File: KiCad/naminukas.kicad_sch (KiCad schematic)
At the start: 13 parts

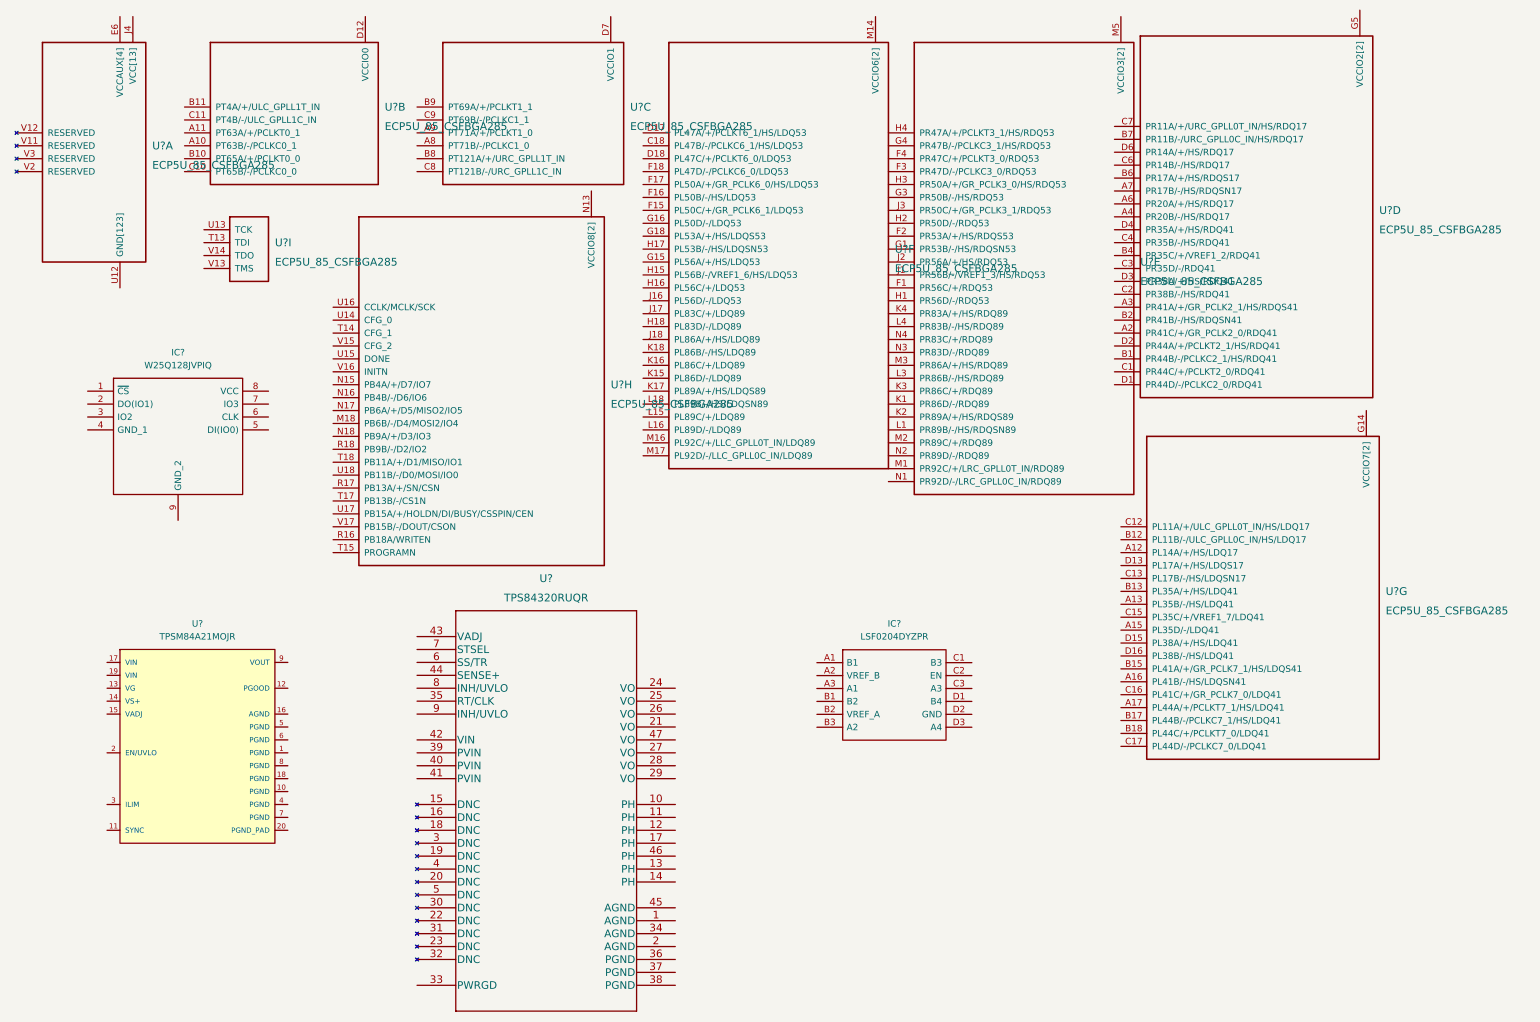
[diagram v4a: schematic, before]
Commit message: Split schematic as both FPGA and power module symbols are huge
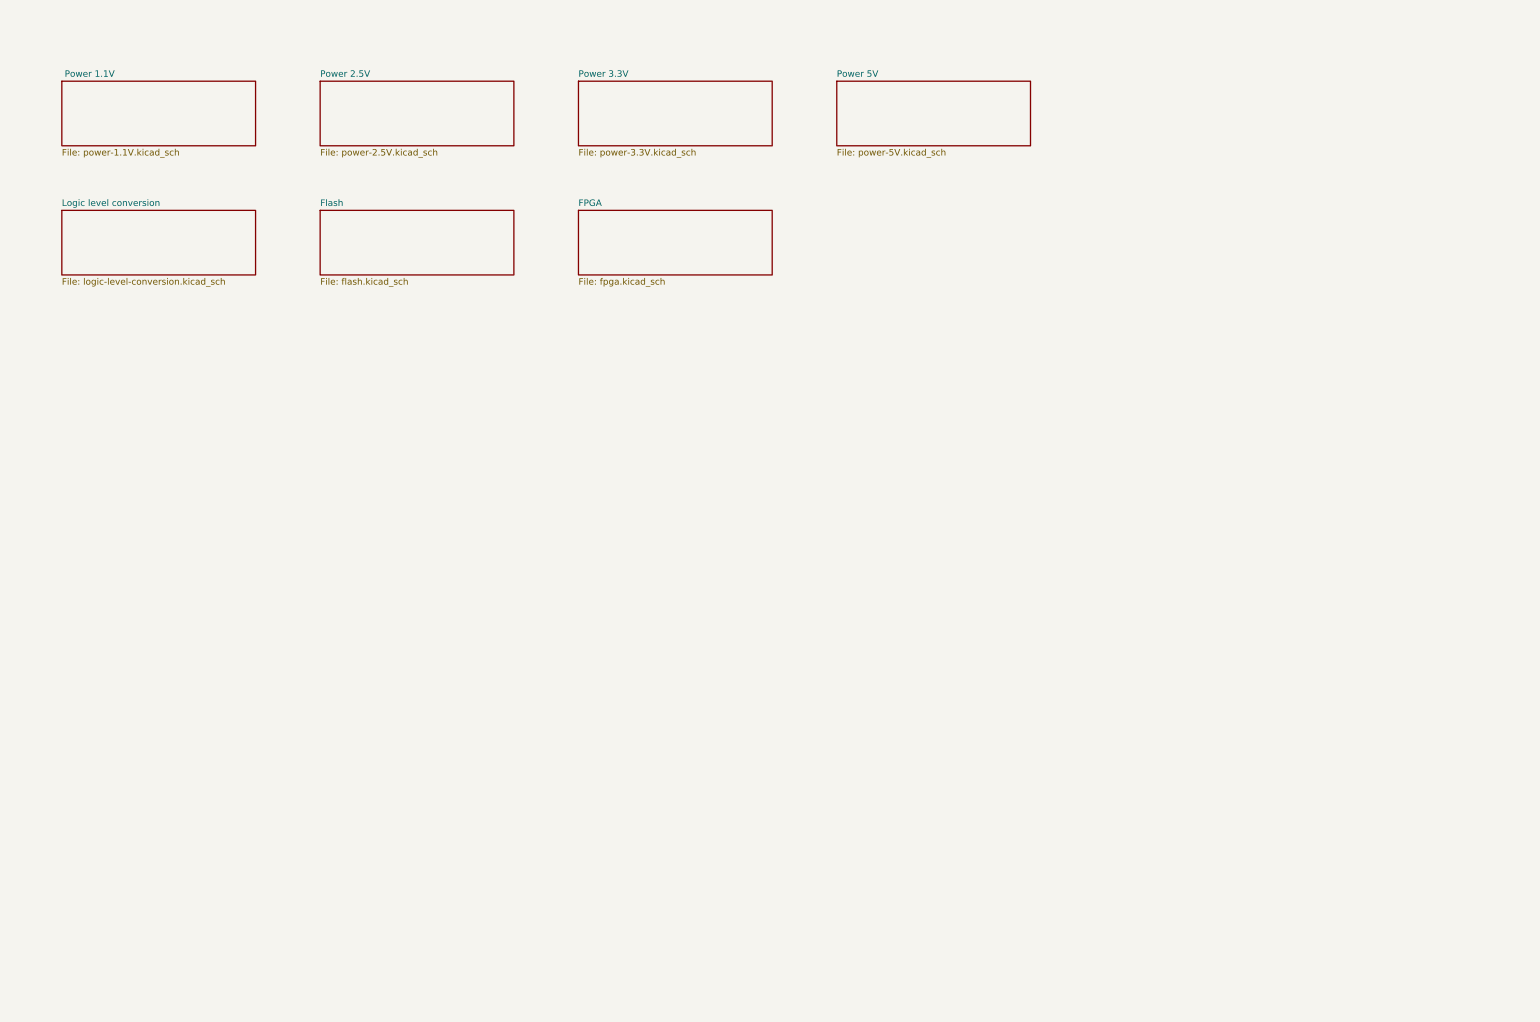
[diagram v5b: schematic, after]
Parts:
- removed IC?: W25Q128JVPIQ, SON127P800X600X80-9N-D, symbol SPI Flash:W25Q128JVPIQ
- removed IC?: LSF0204DYZPR, BGA12C50P3X4_144X194X50, symbol Voltage Level Translator:LSF0204DYZPR
- removed U? (x7): ECP5U_85_CSFBGA285, symbol ECP5:ECP5U_85_CSFBGA285
- removed U?: TPSM84A21MOJR, Texas_Instruments-MOJ0020A-0-0-*, symbol Buck (build-in caps):TPSM84A21MOJR
- removed U?: TPS84320RUQR, RUQ_47, symbol Buck converter:TPS84320RUQR
- removed U? (x2): ECP5U_85_CSFBGA285, ECP5:BGA285C50P18X18_1000X1000X130, symbol ECP5:ECP5U_85_CSFBGA285
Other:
- added sheet  Power 1.1V (power-1.1V.kicad_sch)
- added sheet FPGA (fpga.kicad_sch)
- added sheet Flash (flash.kicad_sch)
- added sheet Logic level conversion (logic-level-conversion.kicad_sch)
- added sheet Power 2.5V (power-2.5V.kicad_sch)
- added sheet Power 3.3V (power-3.3V.kicad_sch)
- added sheet Power 5V (power-5V.kicad_sch)
